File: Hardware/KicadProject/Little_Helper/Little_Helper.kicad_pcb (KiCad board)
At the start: 4 copper layers, 84 x 25.6 mm, 36 parts, among them J1 USB_B_Micro_Molex_1050171001_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, J2 Conn_01x02_Pin, Q1 DMG3415U, SW1 SW_Push, SW2 SW_Push, SW3 SW_Push, SW4 SW_Push, SW5 SW_Push, SW6 SW_SPST, SW7 SW_Push, SW8 SW_Push, U1 AP2112K-3.3, U2 ESP32-S3-MINI-1, U3 MCP73831-2-OT

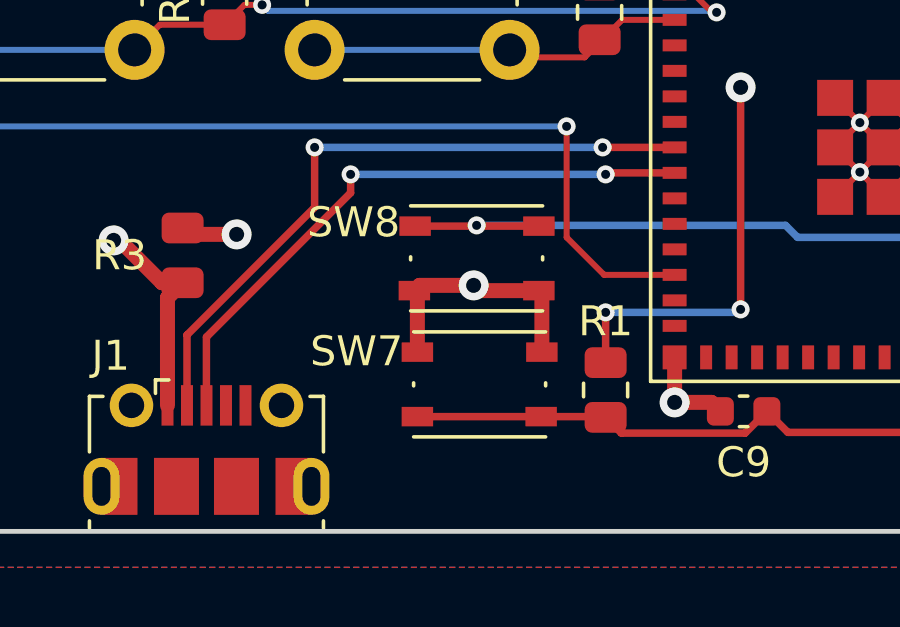
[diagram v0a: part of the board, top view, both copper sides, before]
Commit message: Change Putton Switch
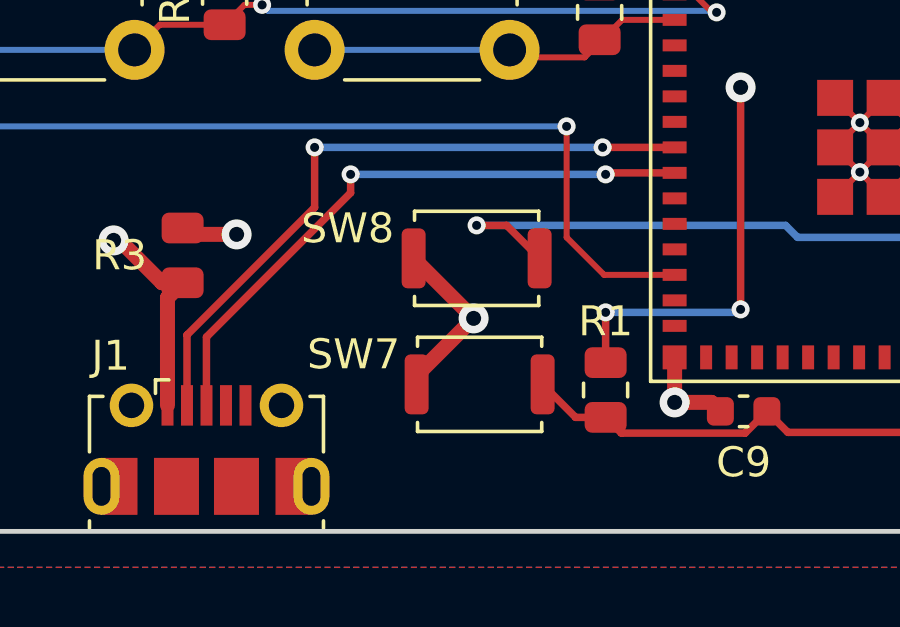
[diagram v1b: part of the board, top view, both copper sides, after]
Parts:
- SW7, SW8: footprint Button_Switch_SMD:SW_Push_1P1T_NO_Vertical_Wuerth_434133025816 -> Button_Switch_SMD:SW_Push_SPST_NO_Alps_SKRK
- turned SW8 to 0 degrees
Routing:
- net /RESET: track 24.3 -> 20.6 mm
- net GND: track 125.8 -> 123.1 mm
- net /BOOT0: track 31.0 -> 29.4 mm

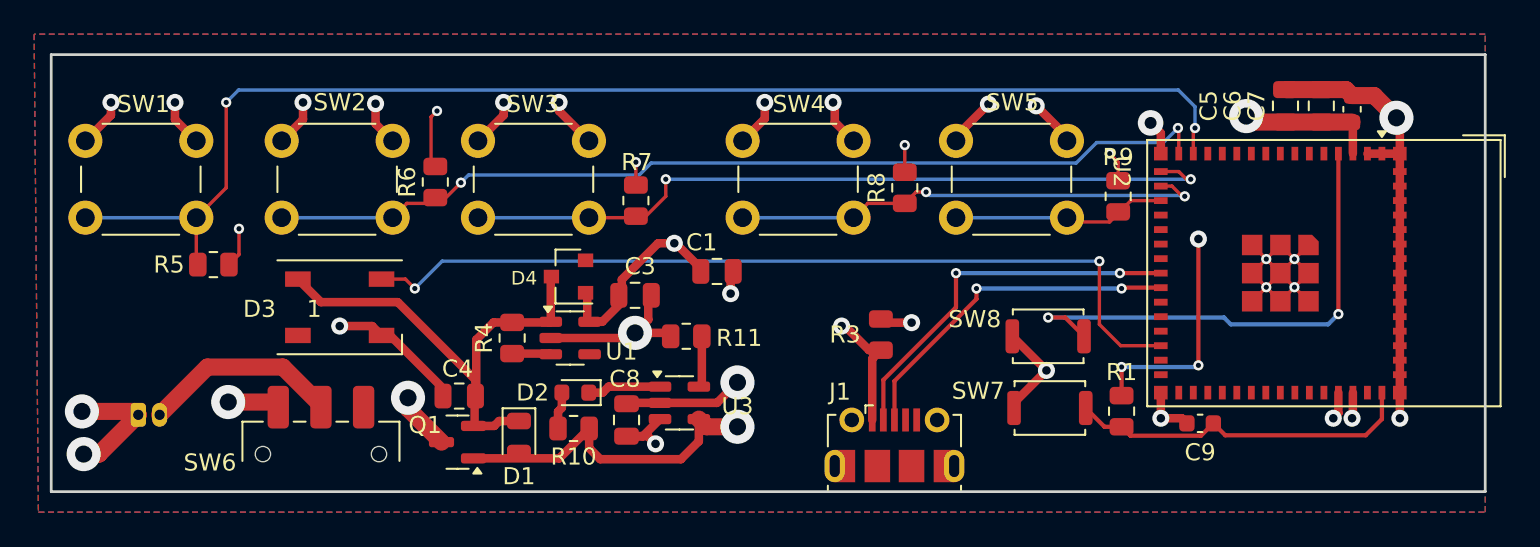
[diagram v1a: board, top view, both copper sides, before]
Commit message: Change Boot and Reset BTN
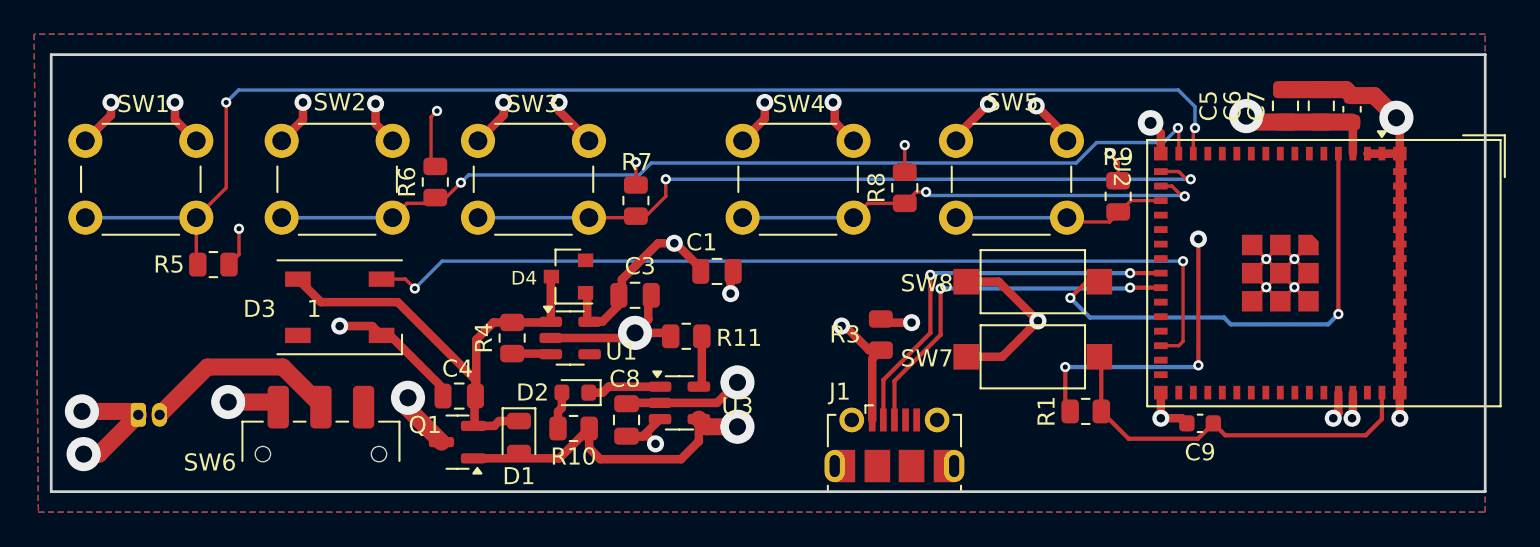
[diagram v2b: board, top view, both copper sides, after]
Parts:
- SW7, SW8: footprint Button_Switch_SMD:SW_Push_SPST_NO_Alps_SKRK -> Button_Switch_SMD:SW_SPST_CK_RS282G05A3
- moved SW8 3.32 mm to (15.5, 0.50)
- moved SW7 3.16 mm to (15.5, 4.90)
- moved R1 2.10 mm to (18.6, 8.10), turned to 0 degrees
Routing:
- net GND: track 123.1 -> 127.7 mm
- net +3.3V: track 44.8 -> 49.2 mm
- net /NEOPIX: track 50.8 -> 53.9 mm
- net /RESET: track 20.6 -> 23.0 mm
- net /Usb_D+: track 20.5 -> 21.7 mm
- net /BOOT0: track 29.4 -> 28.5 mm
- net /Usb_D-: track 22.4 -> 23.2 mm

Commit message: pcb layout v1.0 done
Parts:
- added J3: SOLDER_CON_5x2_TOP, ba_connector:solder_con_5x2_top, F.Cu at (-33.8, 8.70)
- added MH1: fit_3_1, ba_mechanic:fit_3_1, F.Cu at (-38.4, 1.10)
- D1: footprint Diode_SMD:D_0805_2012Metric -> Diode_SMD:D_SOD-123
- J2: value Conn_01x02_Pin -> SOLDER_CON_5x2_TOP; footprint Connector_Hirose:Hirose_DF13-02P-1.25DSA_1x02_P1.25mm_Vertical -> ba_connector:solder_con_5x2_top; moved to F.Cu
- R3: value R2012_100K -> 100k; footprint ba_res:r2012 -> Resistor_SMD:R_0805_2012Metric
- SW6: value SW_SPST -> SW_On_On; footprint Button_Switch_SMD:SW_SPDT_CK_JS102011SAQN -> Button_Switch_SMD:SW_SPDT_PCM12
- SW7, SW8: value SW_Push -> SW_Tactile_Small; footprint Button_Switch_SMD:SW_SPST_CK_RS282G05A3 -> Button_Switch_SMD_JLCPCB:SW_SPST_TS-1088-AR02016
- moved SW8 2.43 mm to (17.9, 0.90)
- moved SW7 2.40 mm to (17.9, 4.80)
- moved J2 0.45 mm to (-37.1, 8.70), turned to 90 degrees
- moved SW6 0.42 mm to (-25.8, 10.7)
- moved D1 0.40 mm to (-14.6, 9.20)
- turned R3 to -90 degrees
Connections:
- D4 pad 2: (no net) -> unconnected-(D4-Pad2)
- R3 pad 1: VBUS -> GND
- R3 pad 2: GND -> VBUS
- SW6 pad 1: +BATT -> unconnected-(SW6-A-Pad1)
- SW6 pad 2: Net-(J2-Pin_2) -> Net-(J3-P1)
- SW6 pad 3: (no net) -> +BATT
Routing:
- net Net-(J2-Pin_2): track 11.7 -> 0.00 mm
- net Net-(J3-P1): track 0.00 -> 11.0 mm
- net GND: track 127.7 -> 121.8 mm
- net /BOOT0: track 28.5 -> 24.8 mm
- net +3.3V: track 49.2 -> 48.1 mm
- net +BATT: track 10.5 -> 11.4 mm, vias 3 -> 2
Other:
- board text added: "+"
- board text added: "-"
- board text added: "WOLKE Little Helper V1.0"
- board text added: "bot."
- board text added: "top."
